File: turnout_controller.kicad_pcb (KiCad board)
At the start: 2 copper layers, 25.4 x 12.7 mm, 30 parts, among them J1 DCC_A, J2 DCC_B, J3 PROG, J4 MOT_CNTL, J5 MOT_POWER, J6 MOT_GND, J7 LED_1, J8 LED_2, SW1 SW_Push, SW2 SW_Push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

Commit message: Silk Screen update. Final change before production
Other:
- board text added: "KHE 2018"
- board text added: "T/O Controller Ver 1.0"
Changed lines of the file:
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@@
     (links 49)
     (no_connects 0)
-    (area 76.362372 64.0829 148.297532 92.7231)
+    (area 104.924999 70.124999 130.475001 82.975001)
     (thickness 1.6)
-    (drawings 4)
+    (drawings 6)
     (tracks 214)
     (zones 0)
@@
     (0 F.Cu signal)
     (31 B.Cu signal)
-    (32 B.Adhes user)
-    (33 F.Adhes user)
-    (34 B.Paste user)
-    (35 F.Paste user)
+    (32 B.Adhes user hide)
+    (33 F.Adhes user hide)
+    (34 B.Paste user hide)
+    (35 F.Paste user hide)
     (36 B.SilkS user)
     (37 F.SilkS user)
-    (38 B.Mask user)
-    (39 F.Mask user)
-    (40 Dwgs.User user)
-    (41 Cmts.User user)
-    (42 Eco1.User user)
-    (43 Eco2.User user)
+    (38 B.Mask user hide)
+    (39 F.Mask user hide)
+    (40 Dwgs.User user hide)
+    (41 Cmts.User user hide)
+    (42 Eco1.User user hide)
+    (43 Eco2.User user hide)
     (44 Edge.Cuts user)
-    (45 Margin user)
-    (46 B.CrtYd user)
-    (47 F.CrtYd user)
-    (48 B.Fab user)
-    (49 F.Fab user)
+    (45 Margin user hide)
+    (46 B.CrtYd user hide)
+    (47 F.CrtYd user hide)
+    (48 B.Fab user hide)
+    (49 F.Fab user hide)
   )
   (setup
@@
     (pad_to_mask_clearance 0.2)
     (aux_axis_origin 0 0)
-    (visible_elements FFFF7F7F)
+    (visible_elements FFFF070D)
     (pcbplotparams
       (layerselection 0x00030_80000001)
@@
     (pad "" np_thru_hole circle (at 0 0) (size 1 1) (drill 1) (layers *.Cu *.Mask))
   )
+  (gr_text "T/O Controller Ver 1.0" (at 107.9881 82.169) (layer B.SilkS)
+    (effects (font (size 0.25 0.25) (thickness 0.03175)) (justify mirror))
+  )
+  (gr_text "KHE 2018" (at 118.1608 76.708) (layer F.SilkS)
+    (effects (font (size 0.25 0.25) (thickness 0.03175)))
+  )
   (gr_line (start 105 82.9) (end 105 70.2) (angle 90) (layer Edge.Cuts) (width 0.15))

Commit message: Submitted for production
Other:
- board text added: "5V"
- board text added: "A"
- board text added: "B"
- board text added: "CLK"
- board text added: "D3"
- board text added: "D4"
- board text added: "GND"
- board text added: "IO"
- board text added: "KEY_DN"
- board text added: "KEY_UP"

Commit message: Updated schematic for clarity. New Netlist. No PCB changes.
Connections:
- net Net-(J4-Pad1) renamed /MOT_CNTL

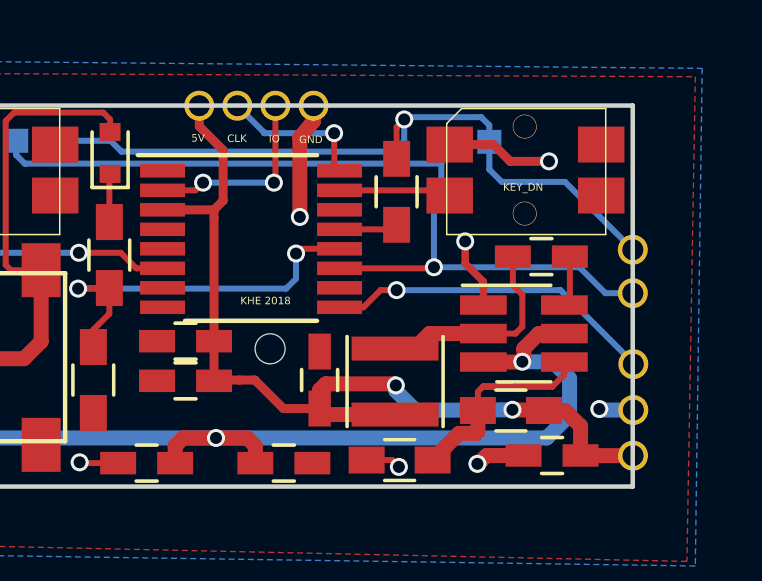
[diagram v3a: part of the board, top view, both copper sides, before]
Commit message: Updated schematics and board layout to fix LED issue
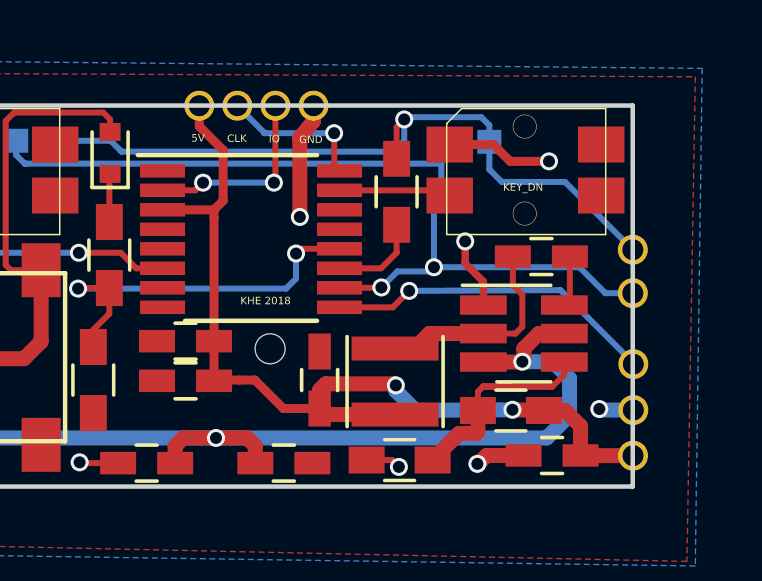
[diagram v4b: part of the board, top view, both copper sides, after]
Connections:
- U2 pad 10: Net-(U2-Pad10) -> /LED2
- U2 pad 11: /LED2 -> Net-(R5-Pad1)
- U2 pad 13: Net-(R5-Pad1) -> Net-(U2-Pad13)
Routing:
- net Net-(R5-Pad1): track 1.96 -> 3.26 mm
- net /LED2: track 29.2 -> 29.5 mm, vias 1 -> 2
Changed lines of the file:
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@@
     (thickness 1.6)
     (drawings 16)
-    (tracks 212)
+    (tracks 218)
     (zones 0)
     (modules 30)
@@
   )
   (setup
-    (last_trace_width 0.25)
+    (last_trace_width 0.2)
     (user_trace_width 0.2)
     (user_trace_width 0.25)
@@
     (pad_to_mask_clearance 0.2)
     (aux_axis_origin 0 0)
-    (visible_elements FFFF476D)
+    (visible_elements FFFFCF6D)
     (pcbplotparams
       (layerselection 0x010f0_80000001)
@@
   (net 17 "Net-(U2-Pad1)")
   (net 18 "Net-(U2-Pad8)")
-  (net 19 "Net-(U2-Pad10)")
-  (net 20 "Net-(U2-Pad14)")
-  (net 21 "Net-(U2-Pad7)")
-  (net 22 "Net-(U2-Pad5)")
-  (net 23 /SWD_CLK)
-  (net 24 /MOT_CNTL)
+  (net 19 "Net-(U2-Pad14)")
+  (net 20 "Net-(U2-Pad7)")
+  (net 21 "Net-(U2-Pad5)")
+  (net 22 /SWD_CLK)
+  (net 23 /MOT_CNTL)
+  (net 24 "Net-(U2-Pad13)")
   (net_class Default "This is the default net class."
     (clearance 0.2)
@@
     (add_net "Net-(R5-Pad1)")
     (add_net "Net-(U2-Pad1)")
-    (add_net "Net-(U2-Pad10)")
+    (add_net "Net-(U2-Pad13)")
     (add_net "Net-(U2-Pad14)")
     (add_net "Net-(U2-Pad5)")
@@
       (net 11 /SWD_IO))
     (pad 3 thru_hole oval (at 0 2.54 270) (size 1 1) (drill 0.7) (layers *.Cu *.Mask)
-      (net 23 /SWD_CLK))
+      (net 22 /SWD_CLK))
     (pad 4 thru_hole oval (at 0 3.81 270) (size 1 1) (drill 0.7) (layers *.Cu *.Mask)
       (net 5 5V))
@@
     )
     (pad 1 thru_hole oval (at 0 0) (size 1 1) (drill 0.7) (layers *.Cu *.Mask)
-      (net 24 /MOT_CNTL))
+      (net 23 /MOT_CNTL))
     (model ${KISYS3DMOD}/Socket_Strips.3dshapes/Socket_Strip_Straight_1x02_Pitch1.27mm.wrl
       (at (xyz 0 0 0))
@@
       (net 1 GND))
     (pad 5 smd rect (at -2.95 0.325) (size 1.5 0.45) (layers F.Cu F.Paste F.Mask)
-      (net 22 "Net-(U2-Pad5)"))
+      (net 21 "Net-(U2-Pad5)"))
     (pad 6 smd rect (at -2.95 0.975) (size 1.5 0.45) (layers F.Cu F.Paste F.Mask)
       (net 12 /KEY_UP))
     (pad 7 smd rect (at -2.95 1.625) (size 1.5 0.45) (layers F.Cu F.Paste F.Mask)
-      (net 21 "Net-(U2-Pad7)"))
+      (net 20 "Net-(U2-Pad7)"))
     (pad 8 smd rect (at -2.95 2.275) (size 1.5 0.45) (layers F.Cu F.Paste F.Mask)
       (net 18 "Net-(U2-Pad8)"))
     (pad 9 smd rect (at 2.95 2.275) (size 1.5 0.45) (layers F.Cu F.Paste F.Mask)
-      (net 24 /MOT_CNTL))
+      (net 23 /MOT_CNTL))
     (pad 10 smd rect (at 2.95 1.625) (size 1.5 0.45) (layers F.Cu F.Paste F.Mask)
-      (net 19 "Net-(U2-Pad10)"))
+      (net 9 /LED2))
     (pad 11 smd rect (at 2.95 0.975) (size 1.5 0.45) (layers F.Cu F.Paste F.Mask)
-      (net 9 /LED2))
+      (net 15 "Net-(R5-Pad1)"))
     (pad 12 smd rect (at 2.95 0.325) (size 1.5 0.45) (layers F.Cu F.Paste F.Mask)
       (net 13 /DCC_IN))
     (pad 13 smd rect (at 2.95 -0.325) (size 1.5 0.45) (layers F.Cu F.Paste F.Mask)
-      (net 15 "Net-(R5-Pad1)"))
+      (net 24 "Net-(U2-Pad13)"))
     (pad 14 smd rect (at 2.95 -0.975) (size 1.5 0.45) (layers F.Cu F.Paste F.Mask)
-      (net 20 "Net-(U2-Pad14)"))
+      (net 19 "Net-(U2-Pad14)"))
     (pad 15 smd rect (at 2.95 -1.625) (size 1.5 0.45) (layers F.Cu F.Paste F.Mask)
       (net 16 /KEY_DN))
     (pad 16 smd rect (at 2.95 -2.275) (size 1.5 0.45) (layers F.Cu F.Paste F.Mask)
-      (net 23 /SWD_CLK))
+      (net 22 /SWD_CLK))
     (model ${KISYS3DMOD}/Housings_SSOP.3dshapes/TSSOP-16_4.4x5mm_Pitch0.65mm.wrl
       (at (xyz 0 0 0))
@@
   (segment (start 106.48 80.2672) (end 106.48 81.51) (width 0.5) (layer F.Cu) (net 8))
   (segment (start 105.9942 79.7814) (end 106.48 80.2672) (width 0.5) (layer F.Cu) (net 8))
+  (segment (start 120.6282 76.2756) (end 122.0095 76.2756) (width 0.2) (layer F.Cu) (net 9))
+  (segment (start 123.6345 75.7301) (end 123.7742 75.5904) (width 0.2) (layer B.Cu) (net 9))
+  (segment (start 122.555 75.7301) (end 123.6345 75.7301) (width 0.2) (layer B.Cu) (net 9))
+  (segment (start 122.0216 76.2635) (end 122.555 75.7301) (width 0.2) (layer B.Cu) (net 9))
+  (via (at 122.0216 76.2635) (size 0.6) (drill 0.4) (layers F.Cu B.Cu) (net 9))
+  (segment (start 122.0095 76.2756) (end 122.0216 76.2635) (width 0.2) (layer F.Cu) (net 9))
   (segment (start 124.02 72.6948) (end 124.02 72.8554) (width 0.2) (layer B.Cu) (net 9))
-  (segment (start 123.7742 73.1012) (end 123.7742 75.5904) (width 0.2) (layer B.Cu) (net 9))
   (segment (start 124.02 72.8554) (end 123.7742 73.1012) (width 0.2) (layer B.Cu) (net 9))
   (segment (start 109.85 71.8312) (end 109.85 71.8516) (width 0.2) (layer B.Cu) (net 9))
@@
   (segment (start 128.6256 75.5904) (end 129.4892 76.454) (width 0.2) (layer B.Cu) (net 9))
   (segment (start 129.4892 76.454) (end 130.4036 76.454) (width 0.2) (layer B.Cu) (net 9))
-  (segment (start 120.6282 75.6256) (end 123.739 75.6256) (width 0.2) (layer F.Cu) (net 9))
   (segment (start 124.02 72.6948) (end 124.02 72.136) (width 0.2) (layer B.Cu) (net 9))
   (segment (start 124.02 72.136) (end 124.02 71.41) (width 0.2) (layer B.Cu) (net 9))
+  (segment (start 123.7742 73.1012) (end 123.7742 75.5904) (width 0.2) (layer B.Cu) (net 9))
   (via (at 123.7742 75.5904) (size 0.6) (drill 0.4) (layers F.Cu B.Cu) (net 9))
   (segment (start 123.739 75.6256) (end 123.7742 75.5904) (width 0.2) (layer F.Cu) (net 9))
@@
   (segment (start 125.3998 79.5782) (end 125.2396 79.7384) (width 0.2) (layer F.Cu) (net 14))
   (segment (start 126.4158 79.5528) (end 125.4252 79.5528) (width 0.2) (layer F.Cu) (net 14))
-  (segment (start 120.6282 74.3256) (end 122.3798 74.3256) (width 0.2) (layer F.Cu) (net 15))
+  (segment (start 120.6282 75.6256) (end 122.0118 75.6256) (width 0.2) (layer F.Cu) (net 15))
+  (segment (start 122.5296 75.1078) (end 122.5296 74.1758) (width 0.2) (layer F.Cu) (net 15))
+  (segment (start 122.0118 75.6256) (end 122.5296 75.1078) (width 0.2) (layer F.Cu) (net 15))
   (segment (start 122.3798 74.3256) (end 122.5296 74.1758) (width 0.2) (layer F.Cu) (net 15))
   (segment (start 120.6282 73.0256) (end 124.1256 73.0256) (width 0.2) (layer F.Cu) (net 16))
   (segment (start 124.1256 73.0256) (end 124.3 73.2) (width 0.2) (layer F.Cu) (net 16))
-  (segment (start 117.221 70.2056) (end 118.1354 71.12) (width 0.2) (layer B.Cu) (net 23))
-  (segment (start 118.11 71.0946) (end 118.11 71.12) (width 0.2) (layer B.Cu) (net 23))
-  (segment (start 118.1354 71.12) (end 118.11 71.0946) (width 0.2) (layer B.Cu) (net 23))
-  (segment (start 120.6282 72.3756) (end 120.4578 72.3756) (width 0.2) (layer F.Cu) (net 23))
-  (segment (start 120.4578 72.3756) (end 120.4468 71.12) (width 0.2) (layer F.Cu) (net 23))
-  (segment (start 120.4468 71.12) (end 118.11 71.12) (width 0.2) (layer B.Cu) (net 23))
-  (via (at 120.4468 71.12) (size 0.6) (drill 0.4) (layers F.Cu B.Cu) (net 23))
-  (segment (start 120.6282 76.9256) (end 121.423 76.9256) (width 0.2) (layer F.Cu) (net 24))
-  (segment (start 127.9906 76.3524) (end 130.42 78.7818) (width 0.2) (layer B.Cu) (net 24))
-  (segment (start 122.5296 76.3524) (end 127.9906 76.3524) (width 0.2) (layer B.Cu) (net 24))
-  (via (at 122.5296 76.3524) (size 0.6) (drill 0.4) (layers F.Cu B.Cu) (net 24))
-  (segment (start 121.9962 76.3524) (end 122.5296 76.3524) (width 0.2) (layer F.Cu) (net 24))
-  (segment (start 121.423 76.9256) (end 121.9962 76.3524) (width 0.2) (layer F.Cu) (net 24))
-  (segment (start 130.42 78.7818) (end 130.42 78.82) (width 0.2) (layer B.Cu) (net 24))
+  (segment (start 117.221 70.2056) (end 118.1354 71.12) (width 0.2) (layer B.Cu) (net 22))
+  (segment (start 118.11 71.0946) (end 118.11 71.12) (width 0.2) (layer B.Cu) (net 22))
+  (segment (start 118.1354 71.12) (end 118.11 71.0946) (width 0.2) (layer B.Cu) (net 22))
+  (segment (start 120.6282 72.3756) (end 120.4578 72.3756) (width 0.2) (layer F.Cu) (net 22))
+  (segment (start 120.4578 72.3756) (end 120.4468 71.12) (width 0.2) (layer F.Cu) (net 22))
+  (segment (start 120.4468 71.12) (end 118.11 71.12) (width 0.2) (layer B.Cu) (net 22))
+  (via (at 120.4468 71.12) (size 0.6) (drill 0.4) (layers F.Cu B.Cu) (net 22))
+  (segment (start 120.6282 76.9256) (end 122.4009 76.9256) (width 0.2) (layer F.Cu) (net 23))
+  (segment (start 127.9906 76.3524) (end 130.42 78.7818) (width 0.2) (layer B.Cu) (net 23))
+  (segment (start 122.9487 76.3778) (end 127.9906 76.3524) (width 0.2) (layer B.Cu) (net 23))
+  (via (at 122.9487 76.3778) (size 0.6) (drill 0.4) (layers F.Cu B.Cu) (net 23))
+  (segment (start 122.4009 76.9256) (end 122.9487 76.3778) (width 0.2) (layer F.Cu) (net 23))
+  (segment (start 130.42 78.7818) (end 130.42 78.82) (width 0.2) (layer B.Cu) (net 23))
   (zone (net 1) (net_name GND) (layer F.Cu) (hatch edge 0.508)
     (connect_pads (clearance 0.2))

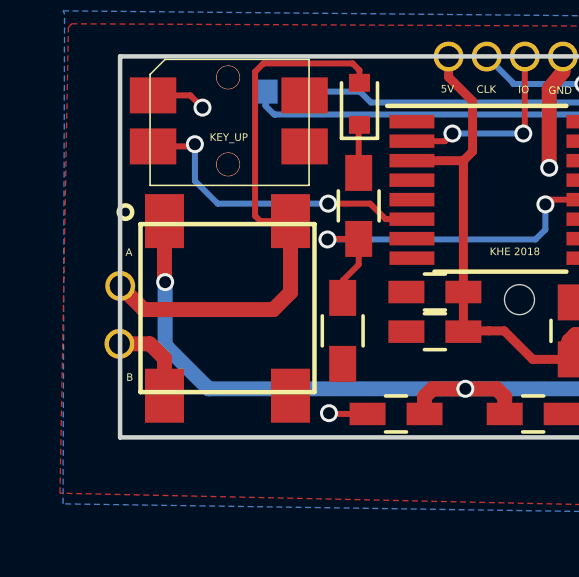
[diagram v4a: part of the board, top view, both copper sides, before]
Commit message: Updated schematics and board layout to fix LED issue
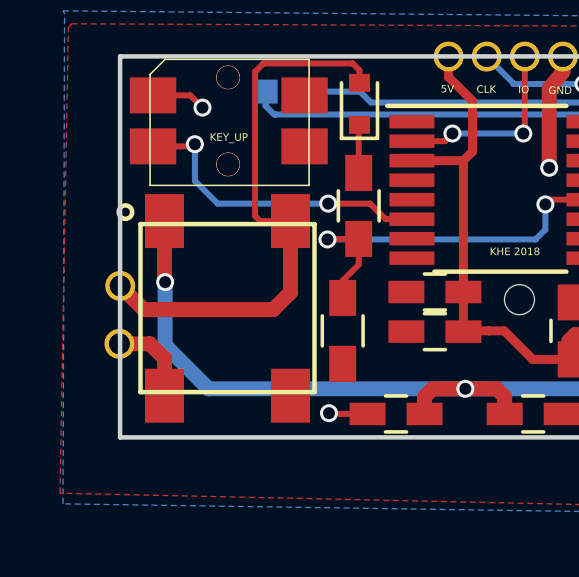
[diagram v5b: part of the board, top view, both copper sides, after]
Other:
- board text added: "DCC-A"
- board text added: "DCC-B"
- board text added: "T/O Controller Ver 1.1"
- board text removed: "A"
- board text removed: "B"
- board text removed: "T/O Controller Ver 1.0"
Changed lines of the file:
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@@
     (pad "" np_thru_hole circle (at 0 0) (size 1 1) (drill 1) (layers *.Cu *.Mask))
   )
-  (gr_text A (at 105.2957 76.7334) (layer F.SilkS)
-    (effects (font (size 0.25 0.25) (thickness 0.03175)))
+  (gr_text DCC-A (at 106.3625 76.6064) (layer B.SilkS)
+    (effects (font (size 0.4 0.4) (thickness 0.03175)) (justify mirror))
   )
-  (gr_text B (at 105.3211 80.899) (layer F.SilkS)
-    (effects (font (size 0.25 0.25) (thickness 0.03175)))
+  (gr_text DCC-B (at 106.3625 81.4197) (layer B.SilkS)
+    (effects (font (size 0.4 0.4) (thickness 0.03175)) (justify mirror))
   )
   (gr_text GND (at 119.6721 71.3359) (layer F.SilkS)
@@
     (effects (font (size 0.25 0.25) (thickness 0.03175)))
   )
-  (gr_text "T/O Controller Ver 1.0" (at 107.9881 82.169) (layer B.SilkS)
+  (gr_text "T/O Controller Ver 1.1" (at 107.9881 82.169) (layer B.SilkS)
     (effects (font (size 0.25 0.25) (thickness 0.03175)) (justify mirror))
   )
